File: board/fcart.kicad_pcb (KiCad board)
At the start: 2 copper layers, 100 x 62.7 mm, 96 parts, among them J1 USB_C_16P, J2 DM3D-SF, J3 JTAG, J4 SWD, J5 Famicom_cartridge, SW1 PTS647SM70, U1 USBLC6-2SC6, U10 W9864G6KH-6, U2 TLV76133DCY, U3 TPS2116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

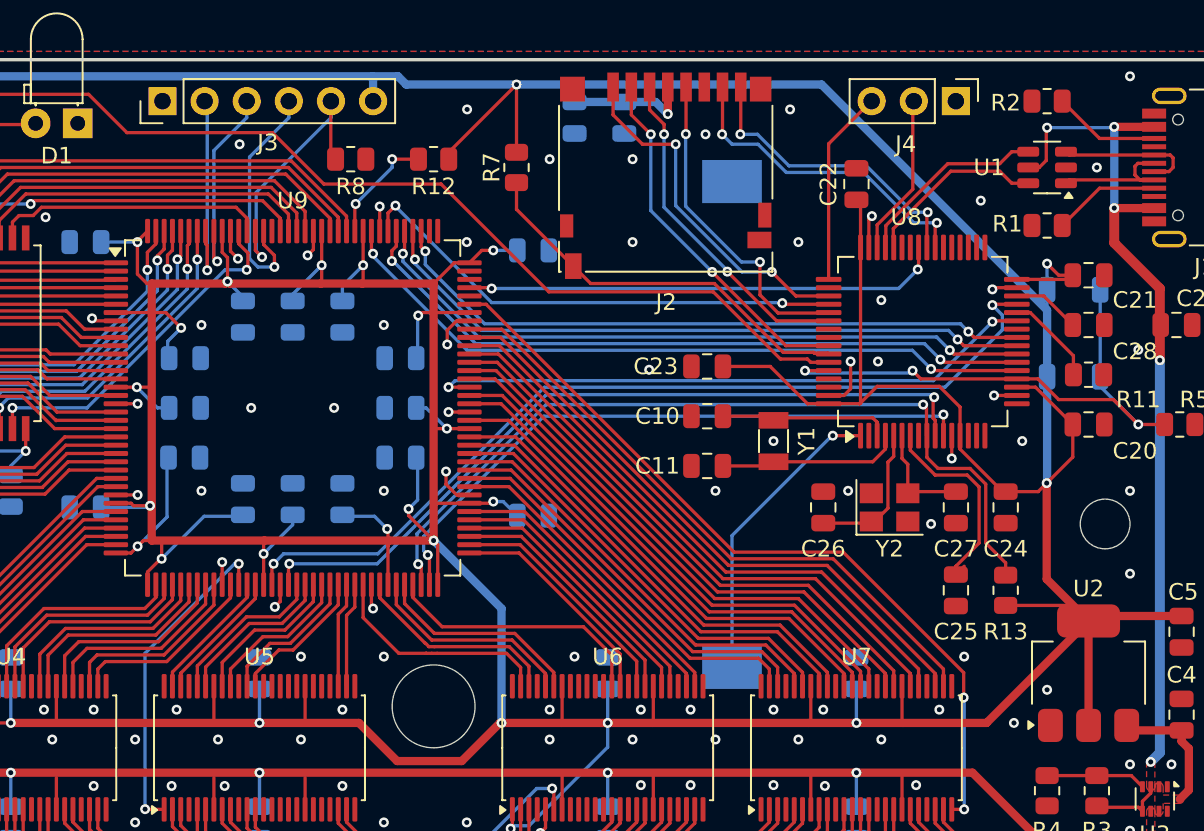
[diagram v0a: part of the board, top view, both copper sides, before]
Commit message: fixes to some tracks
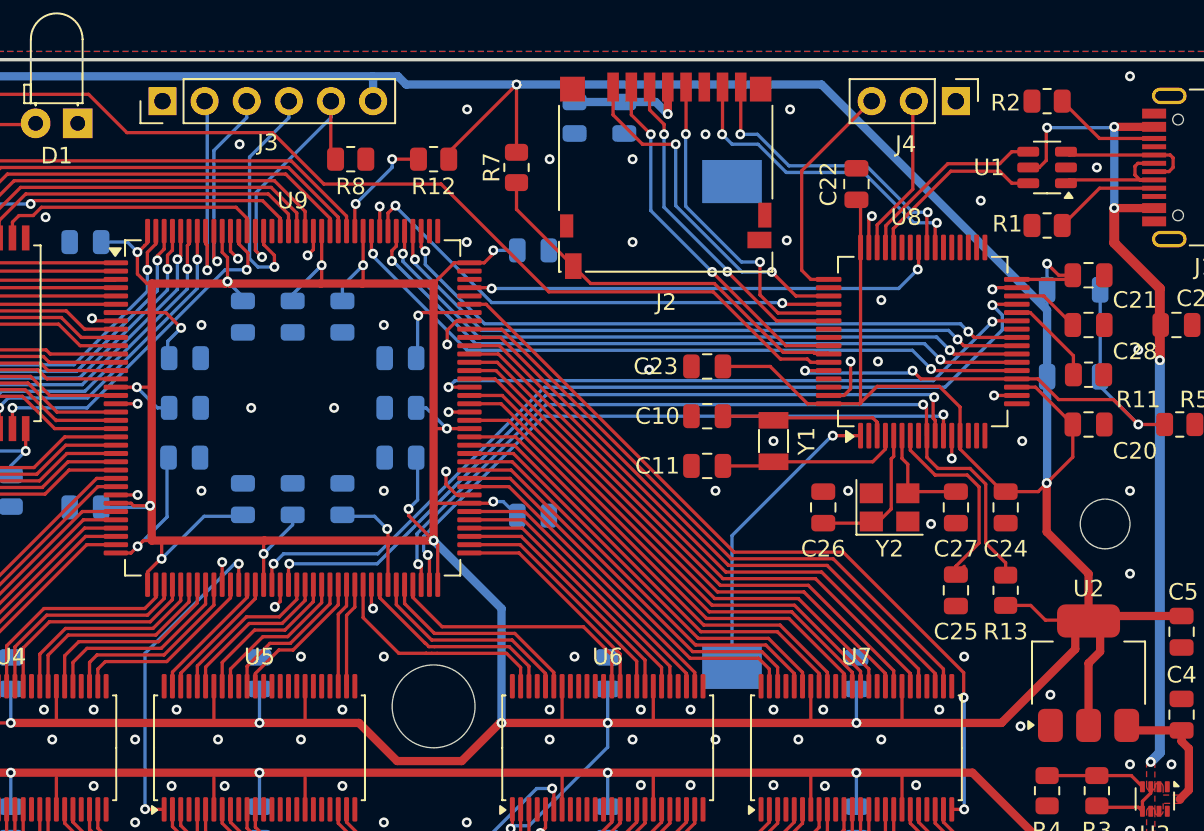
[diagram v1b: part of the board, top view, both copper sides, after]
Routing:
- net SWCLK: track 11.8 -> 13.8 mm
- net +3V3: track 546.9 -> 548.4 mm

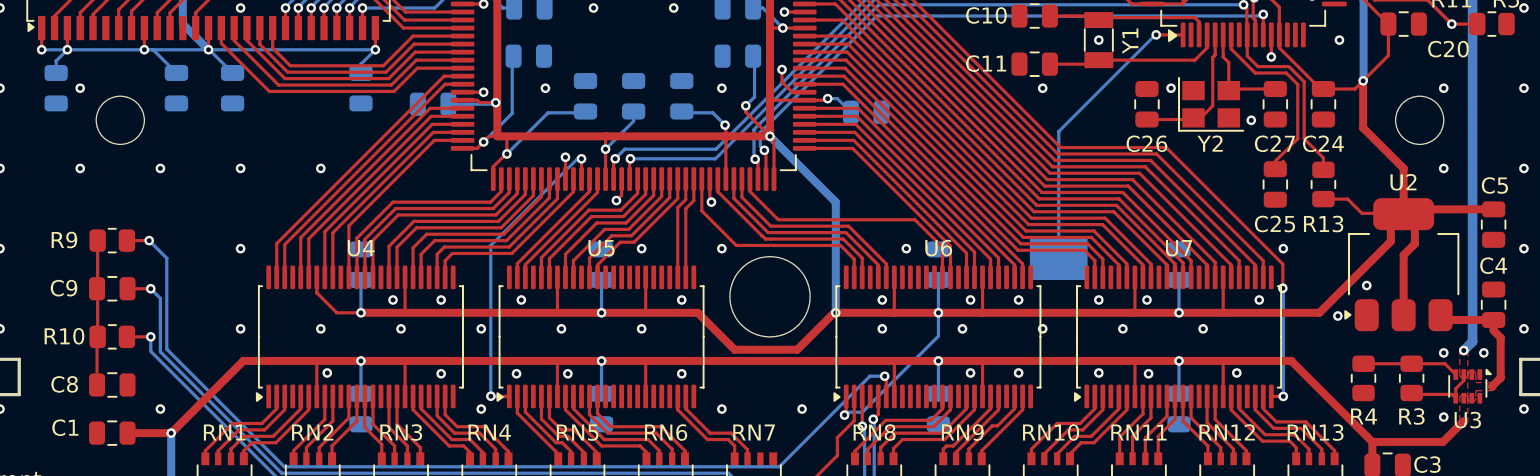
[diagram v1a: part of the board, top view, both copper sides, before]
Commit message: update pcb holes
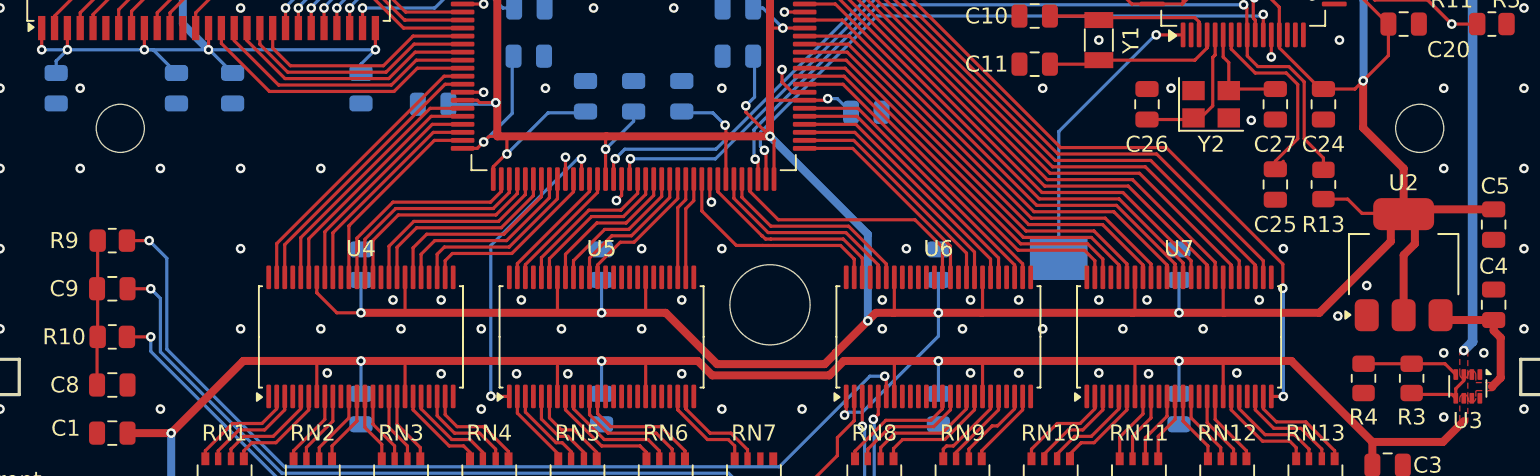
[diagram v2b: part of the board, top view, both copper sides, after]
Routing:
- net +3V3: track 548.4 -> 550.5 mm
- net VCART: track 133.2 -> 133.9 mm

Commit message: optimize for native board
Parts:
- added D3: LTST-S326KGJRKT, LED_SMD:LED_LiteOn_LTST-S326, F.Cu at (130.7, 61.9)
- added J6: MSD-4-A, fcart:microSD_HC_Same_Sky_MSD-4-A, F.Cu at (167.8, 56.7)
- added J8: USB4085, Connector_USB:USB_C_Receptacle_GCT_USB4085, F.Cu at (209.3, 78.4)
- J1: value USB_C_16P -> USB_C_14P
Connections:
- J1 pad A8: unconnected-(J1-SBU1-PadA8) -> (no net)
- J1 pad B8: unconnected-(J1-SBU2-PadB8) -> (no net)
